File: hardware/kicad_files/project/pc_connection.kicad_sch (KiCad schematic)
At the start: 21 parts, among them U4 GT-USB-7010ASV, U5 FT232H

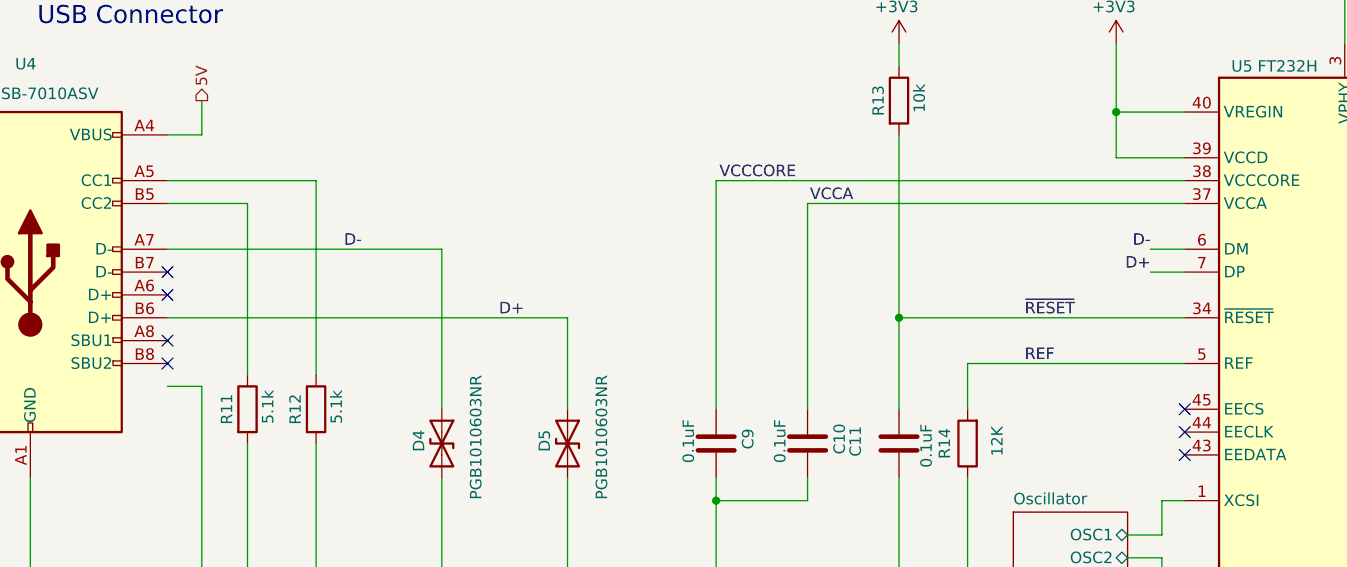
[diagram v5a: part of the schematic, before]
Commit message: fix: add a connection to the addtional D+ and D- terminals to allow a reversible plugging of the connector, route the USB data line using an impedance matched differential pair
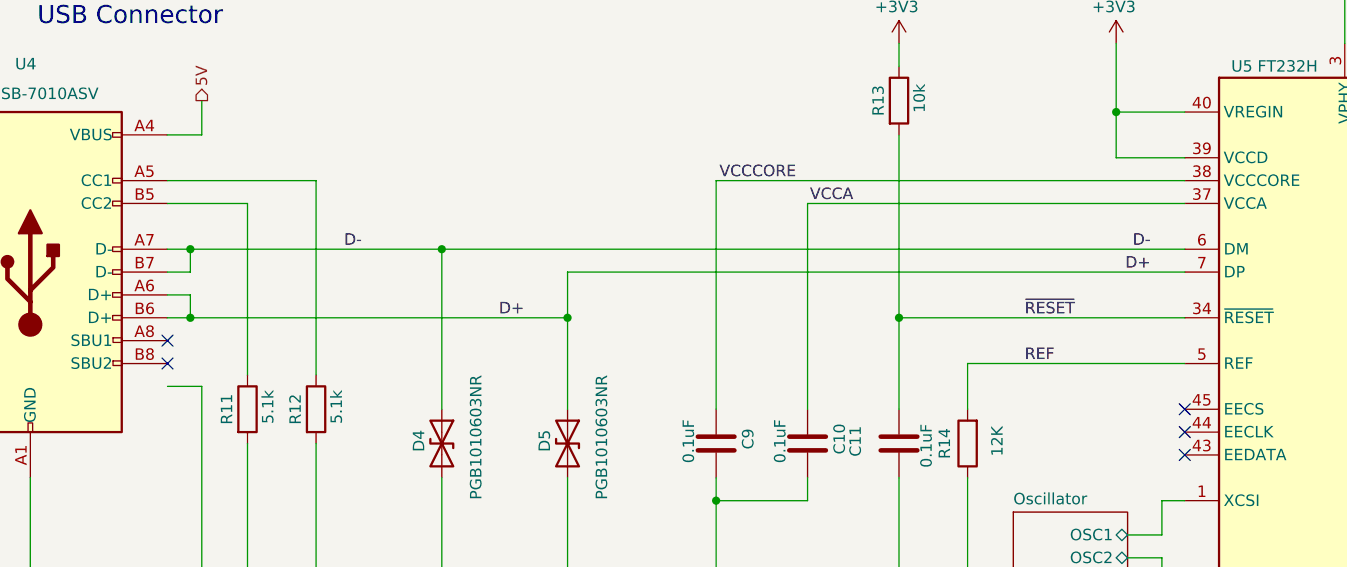
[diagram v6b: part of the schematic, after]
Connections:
- net D+: now also U4.A6 (D+)
- net D-: now also U4.B7 (D-)
- no-connect marks 17 -> 15
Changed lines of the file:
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@@
+	)
+	(junction
+		(at 63.5 96.52)
+		(diameter 0)
+		(color 0 0 0 0)
 	)
 	(junction
@@
 	)
 	(junction
+		(at 91.44 88.9)
+		(diameter 0)
+		(color 0 0 0 0)
+	)
+	(junction
 		(at 205.74 148.59)
 		(diameter 0)
@@
 	(junction
 		(at 203.2 148.59)
+		(diameter 0)
+		(color 0 0 0 0)
+	)
+	(junction
+		(at 105.41 96.52)
+		(diameter 0)
+		(color 0 0 0 0)
+	)
+	(junction
+		(at 63.5 88.9)
 		(diameter 0)
 		(color 0 0 0 0)
@@
 	)
 	(no_connect
-		(at 60.96 91.44)
-	)
-	(no_connect
 		(at 60.96 99.06)
 	)
@@
 	(no_connect
 		(at 219.71 106.68)
-	)
-	(no_connect
-		(at 60.96 93.98)
 	)
 	(no_connect
@@
 	(wire
 		(pts
+			(xy 60.96 93.98) (xy 63.5 93.98)
+		)
+		(stroke
+			(width 0)
+			(type default)
+		)
+	)
+	(wire
+		(pts
 			(xy 208.28 142.24) (xy 208.28 148.59)
 		)
@@
 	(wire
 		(pts
-			(xy 60.96 96.52) (xy 105.41 96.52)
+			(xy 60.96 96.52) (xy 63.5 96.52)
+		)
+		(stroke
+			(width 0)
+			(type default)
+		)
+	)
+	(wire
+		(pts
+			(xy 91.44 88.9) (xy 173.99 88.9)
 		)
 		(stroke
@@
 	(wire
 		(pts
-			(xy 170.18 91.44) (xy 173.99 91.44)
-		)
-		(stroke
-			(width 0)
-			(type default)
-		)
-	)
-	(wire
-		(pts
 			(xy 215.9 54.61) (xy 215.9 52.07)
 		)
@@
 	(wire
 		(pts
-			(xy 60.96 88.9) (xy 91.44 88.9)
+			(xy 60.96 88.9) (xy 63.5 88.9)
 		)
 		(stroke
@@
 	(wire
 		(pts
+			(xy 63.5 88.9) (xy 63.5 91.44)
+		)
+		(stroke
+			(width 0)
+			(type default)
+		)
+	)
+	(wire
+		(pts
 			(xy 142.24 106.68) (xy 142.24 96.52)
 		)
@@
 	(wire
 		(pts
+			(xy 63.5 88.9) (xy 91.44 88.9)
+		)
+		(stroke
+			(width 0)
+			(type default)
+		)
+	)
+	(wire
+		(pts
 			(xy 233.68 52.07) (xy 233.68 54.61)
 		)
@@
 	(wire
 		(pts
-			(xy 170.18 88.9) (xy 173.99 88.9)
+			(xy 60.96 91.44) (xy 63.5 91.44)
+		)
+		(stroke
+			(width 0)
+			(type default)
+		)
+	)
+	(wire
+		(pts
+			(xy 105.41 91.44) (xy 173.99 91.44)
 		)
 		(stroke
@@
 	(wire
 		(pts
+			(xy 63.5 96.52) (xy 105.41 96.52)
+		)
+		(stroke
+			(width 0)
+			(type default)
+		)
+	)
+	(wire
+		(pts
+			(xy 63.5 93.98) (xy 63.5 96.52)
+		)
+		(stroke
+			(width 0)
+			(type default)
+		)
+	)
+	(wire
+		(pts
 			(xy 182.88 151.13) (xy 182.88 148.59)
 		)
@@
 		(pts
 			(xy 215.9 52.07) (xy 207.01 52.07)
+		)
+		(stroke
+			(width 0)
+			(type default)
+		)
+	)
+	(wire
+		(pts
+			(xy 105.41 91.44) (xy 105.41 96.52)
 		)
 		(stroke
@@
 	(label "Shield"
 		(at 38.1 116.84 180)
-		(fields_autoplaced yes)
 		(effects
 			(font
@@
 	(label "TX_LED"
 		(at 231.14 104.14 0)
-		(fields_autoplaced yes)
 		(effects
 			(font
@@
 	(label "~{RESET}"
 		(at 156.21 96.52 0)
-		(fields_autoplaced yes)
 		(effects
 			(font
@@
 	(label "FTDI_SPI.SCK"
 		(at 219.71 73.66 0)
-		(fields_autoplaced yes)
 		(effects
 			(font
@@
 	(label "FTDI_SPI.POCI"
 		(at 219.71 76.2 0)
-		(fields_autoplaced yes)
 		(effects
 			(font
@@
 	(label "D-"
 		(at 82.55 88.9 180)
-		(fields_autoplaced yes)
 		(effects
 			(font
@@
 	(label "D+"
 		(at 170.18 91.44 180)
-		(fields_autoplaced yes)
 		(effects
 			(font
@@
 	(label "RX_LED"
 		(at 231.14 101.6 0)
-		(fields_autoplaced yes)
 		(effects
 			(font
@@
 	(label "REF"
 		(at 156.21 101.6 0)
-		(fields_autoplaced yes)
 		(effects
 			(font
@@
 	(label "FTDI_SPI.CS"
 		(at 219.71 81.28 0)
-		(fields_autoplaced yes)
 		(effects
 			(font
@@
 	(label "D-"
 		(at 170.18 88.9 180)
-		(fields_autoplaced yes)
 		(effects
 			(font
@@
 	(label "D+"
 		(at 97.79 96.52 0)
-		(fields_autoplaced yes)
 		(effects
 			(font
@@
 	(label "FTDI_SPI.PICO"
 		(at 219.71 78.74 0)
-		(fields_autoplaced yes)
 		(effects
 			(font
@@
 	(label "VCCCORE"
 		(at 130.81 81.28 180)
-		(fields_autoplaced yes)
 		(effects
 			(font
@@
 	(label "VCCA"
 		(at 137.16 83.82 180)
-		(fields_autoplaced yes)
 		(effects
 			(font
@@
 		(shape output)
 		(at 223.52 99.06 0)
-		(fields_autoplaced yes)
 		(effects
 			(font
@@
 		(shape output)
 		(at 223.52 96.52 0)
-		(fields_autoplaced yes)
 		(effects
 			(font
@@
 		(shape output)
 		(at 236.22 83.82 0)
-		(fields_autoplaced yes)
 		(effects
 			(font
@@
 		(shape output)
 		(at 64.77 72.39 90)
-		(fields_autoplaced yes)
-		(effects
-			(font
+		(effects
+			(font
